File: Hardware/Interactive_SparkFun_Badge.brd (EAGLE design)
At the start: 88.9 x 63.5 mm, 30 parts, among them J1 AVR_SPI_PRG_6PTH, U1 ATMEGA328P

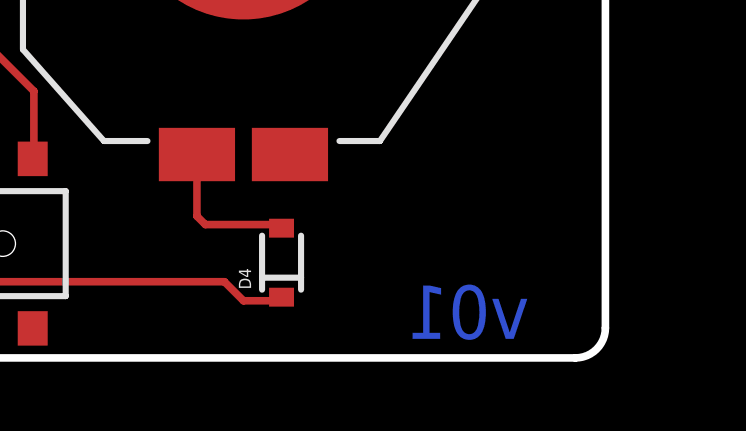
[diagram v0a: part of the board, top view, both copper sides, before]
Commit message: Fixing version number to v10
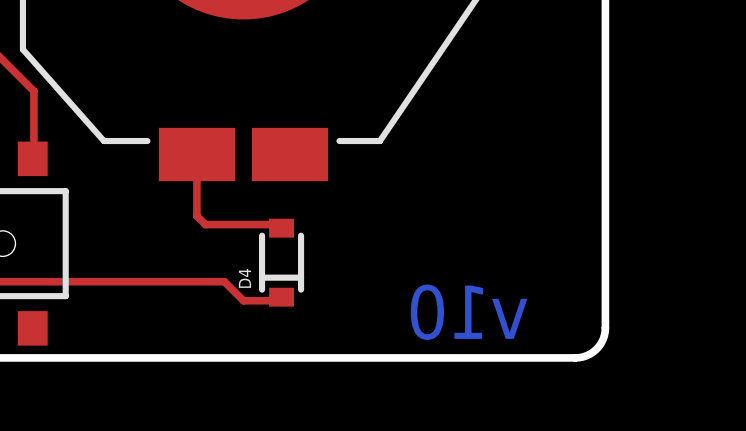
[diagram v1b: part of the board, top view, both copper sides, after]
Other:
- board text added: "v10"
- board text removed: "v01"
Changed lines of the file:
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@@
 <layer number="47" name="Measures" color="7" fill="1" visible="no" active="yes"/>
 <layer number="48" name="Document" color="7" fill="1" visible="no" active="yes"/>
-<layer number="49" name="Reference" color="7" fill="1" visible="yes" active="yes"/>
+<layer number="49" name="Reference" color="7" fill="1" visible="no" active="yes"/>
 <layer number="50" name="dxf" color="7" fill="1" visible="no" active="no"/>
 <layer number="51" name="tDocu" color="6" fill="1" visible="yes" active="yes"/>
@@
 <board>
 <plain>
-<text x="86.36" y="0.635" size="1.778" layer="16" font="vector" ratio="15" rot="MR0">v01</text>
+<text x="86.36" y="0.635" size="1.778" layer="16" font="vector" ratio="15" rot="MR0">v10</text>
 <text x="48.26" y="-8.89" size="1.778" layer="51" font="vector" ratio="15">Toni Klopfenstein</text>
 <text x="3.175" y="29.21" size="1.27" layer="21" font="vector" ratio="15" rot="SR270">3.3V FTDI</text>
